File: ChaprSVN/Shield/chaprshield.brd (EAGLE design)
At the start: 72.7 x 47 mm, 16 parts, among them M2 RN42 Module

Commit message: First version of the ChapR board v0.2.  These files were sent to Sunstone.
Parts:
- removed U$1: VDIP2, ChapR-Custom:VDIP2
- removed U$3: PROMINI, ChapR-Custom:PROMINI
- added ARD: PROMINI, ChapR-Custom:PROMINI
- added JP1: (no value), pinhead:1X02
- added PB1: PUSHBUTTON, ChapR-Custom:2-PIN-PUSHBUTTON
- added R10, R11: 10k, resistor:0207/10
- added VDIP: VDIP2, ChapR-Custom:VDIP2
- moved R9 36.9 mm to (54.6, 36.8)
- moved LED2 31.2 mm to (69.8, 6.35)
- moved R3 26.4 mm to (54.6, 33.0), turned to 0 degrees
- moved LED1 22.9 mm to (69.8, 12.7)
- moved R8 19.1 mm to (44.5, 20.3)
- moved U$2 14.9 mm to (69.8, 36.8)
- moved R7 11.5 mm to (57.1, 20.3)
- moved M2 5.08 mm to (47.0, 10.2)
- moved R2 2.84 mm to (40.6, 30.5)
- moved R1 2.54 mm to (40.6, 35.6)
- moved R5 1.80 mm to (7.62, 16.5)
- moved R4 1.80 mm to (10.2, 14.0)
- moved R6 1.80 mm to (12.7, 11.4)
- moved - 1.53 mm to (64.6, 43.8)
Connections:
- new net N$22: JP1.1, M2.22, R11.2
- new net N$24: ARD.A0, PB1.P$2, R10.2
- net +9V: now also ARD.RAWV; no longer U$3.RAWV
- net 3.3V: now also JP1.2, VDIP.32, VDIP.38, VDIP.39; no longer U$1.32, U$1.38, U$1.39
- net GND: now also ARD.GND, ARD.GND2, R10.1, R11.1, VDIP.12, VDIP.13, VDIP.15, VDIP.26; no longer M2.25, M2.27, U$1.12, U$1.13, U$1.15, U$1.26, U$3.GND, U$3.GND2
- net LED1(BD5): now also VDIP.4; no longer U$1.4
- net LED2(BD6): now also VDIP.5; no longer U$1.5
- net N$1: now also ARD.VCC, PB1.P$1, VDIP.2, VDIP.3, VDIP.9; no longer U$1.2, U$1.3, U$1.9, U$3.VCC
- net N$10: now also ARD.D9, VDIP.18; no longer U$1.18, U$3.D9
- net N$11: now also ARD.D8, VDIP.17; no longer U$1.17, U$3.D8
- net N$12: now also ARD.D7, VDIP.16; no longer U$1.16, U$3.D7
- net N$13: now also ARD.D6, VDIP.14; no longer U$1.14, U$3.D6
- net N$14: now also ARD.D4; no longer U$3.D4
- net N$15: now also ARD.D3; no longer U$3.D3
- net N$18: now also ARD.A2; no longer U$3.A2
- net N$2: now also ARD.D10, VDIP.30; no longer U$1.30, U$3.D10
- net N$20: now also ARD.A1; no longer U$3.A1
- net N$21: now also ARD.A3; no longer U$3.A3
- net N$3: now also ARD.D13; no longer U$3.D13
- net N$4: now also ARD.D12; no longer U$3.D12
- net N$5: now also ARD.D11; no longer U$3.D11
- net N$8: now also ARD.D5; no longer U$3.D5
- net NC(1): now also VDIP.1; no longer U$1.1
- net NC(2): now also VDIP.40; no longer U$1.40
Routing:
- net N$24: track 0.00 -> 97.4 mm, vias 0 -> 2
- net 3.3V: track 51.4 -> 115.2 mm, vias 1 -> 2
- net N$1: track 42.4 -> 102.4 mm, vias 0 -> 2
- net N$22: track 0.00 -> 55.9 mm
- net N$21: track 9.87 -> 62.1 mm, vias 0 -> 2
- net N$9: track 43.8 -> 83.3 mm, vias 0 -> 4
- net N$2: track 57.9 -> 82.5 mm
- net N$19: track 38.0 -> 14.4 mm
- net N$20: track 57.3 -> 33.8 mm
- net GND: track 150.3 -> 171.8 mm
- net N$16: track 37.1 -> 20.6 mm
- net N$15: track 48.8 -> 39.0 mm, vias 0 -> 1
- net N$5: track 72.3 -> 63.2 mm, vias 0 -> 1
- net +9V: track 68.8 -> 60.6 mm, vias 0 -> 3
- net N$11: track 53.7 -> 60.6 mm
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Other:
- board size 72.7 x 47 mm -> 76 x 47 mm
- board text added: "ChapR v0.2"

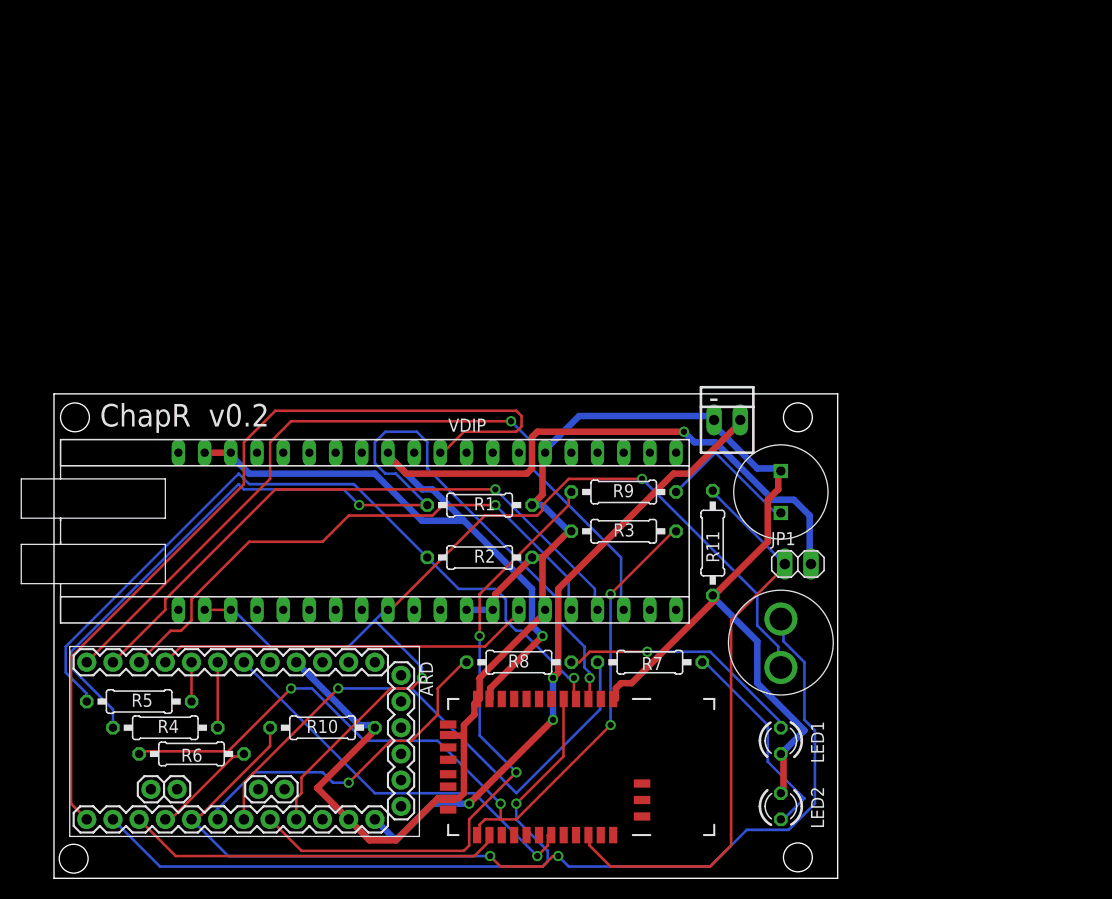
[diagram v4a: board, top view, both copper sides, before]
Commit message: 
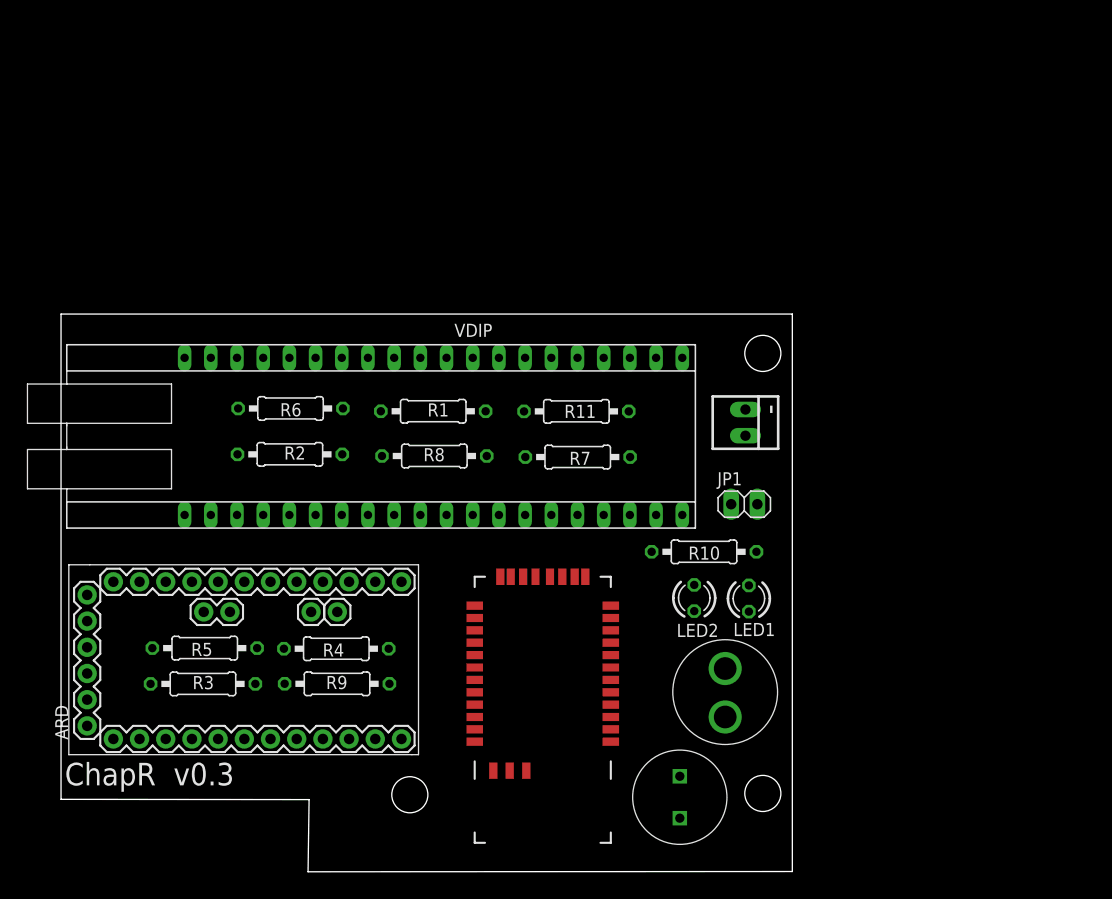
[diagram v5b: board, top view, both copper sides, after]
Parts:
- R1, R2, R3: value 20k -> 19.1k
- moved R3 43.4 mm to (13.8, 18.2)
- moved R10 40.7 mm to (62.4, 31.0), turned to 0 degrees
- moved R6 34.8 mm to (22.3, 44.9)
- moved R9 33.4 mm to (26.8, 18.2)
- moved U$2 31.2 mm to (60.0, 7.23)
- moved LED2 21.9 mm to (61.5, 26.6)
- moved R8 21.6 mm to (36.2, 40.3)
- moved R7 21.1 mm to (50.1, 40.2)
- moved R2 20.9 mm to (22.2, 40.5)
- moved R11 18.4 mm to (50.0, 44.6), turned to 180 degrees
- moved R4 18.3 mm to (26.7, 21.6), turned to 180 degrees
- moved LED1 14.1 mm to (66.8, 26.5), turned to 90 degrees
- moved ARD 10.3 mm to (17.8, 21.8), turned to 90 degrees
- moved R1 10.2 mm to (36.1, 44.7)
- moved VDIP 9.22 mm to (36.2, 42.2)
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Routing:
- net GND: track 171.8 -> 0.00 mm
- net 3.3V: track 115.2 -> 0.00 mm, vias 2 -> 0
- net N$1: track 102.4 -> 0.00 mm, vias 2 -> 0
- net N$6: track 97.4 -> 0.00 mm, vias 2 -> 0
- net N$24: track 97.4 -> 0.00 mm, vias 2 -> 0
- net N$9: track 83.3 -> 0.00 mm, vias 4 -> 0
- net N$2: track 82.5 -> 0.00 mm
- net N$10: track 75.9 -> 0.00 mm, vias 1 -> 0
- net N$7: track 74.0 -> 0.00 mm, vias 1 -> 0
- net N$5: track 63.2 -> 0.00 mm, vias 1 -> 0
- net N$21: track 62.1 -> 0.00 mm, vias 2 -> 0
- net +9V: track 60.6 -> 0.00 mm, vias 3 -> 0
- net N$11: track 60.6 -> 0.00 mm, vias 1 -> 0
- net N$22: track 55.9 -> 0.00 mm
- net N$12: track 55.4 -> 0.00 mm, vias 1 -> 0
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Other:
- board size 76 x 47 mm -> 70.9 x 54.1 mm
- board text added: "ChapR v0.3"
- board text removed: "ChapR v0.2"

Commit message: 
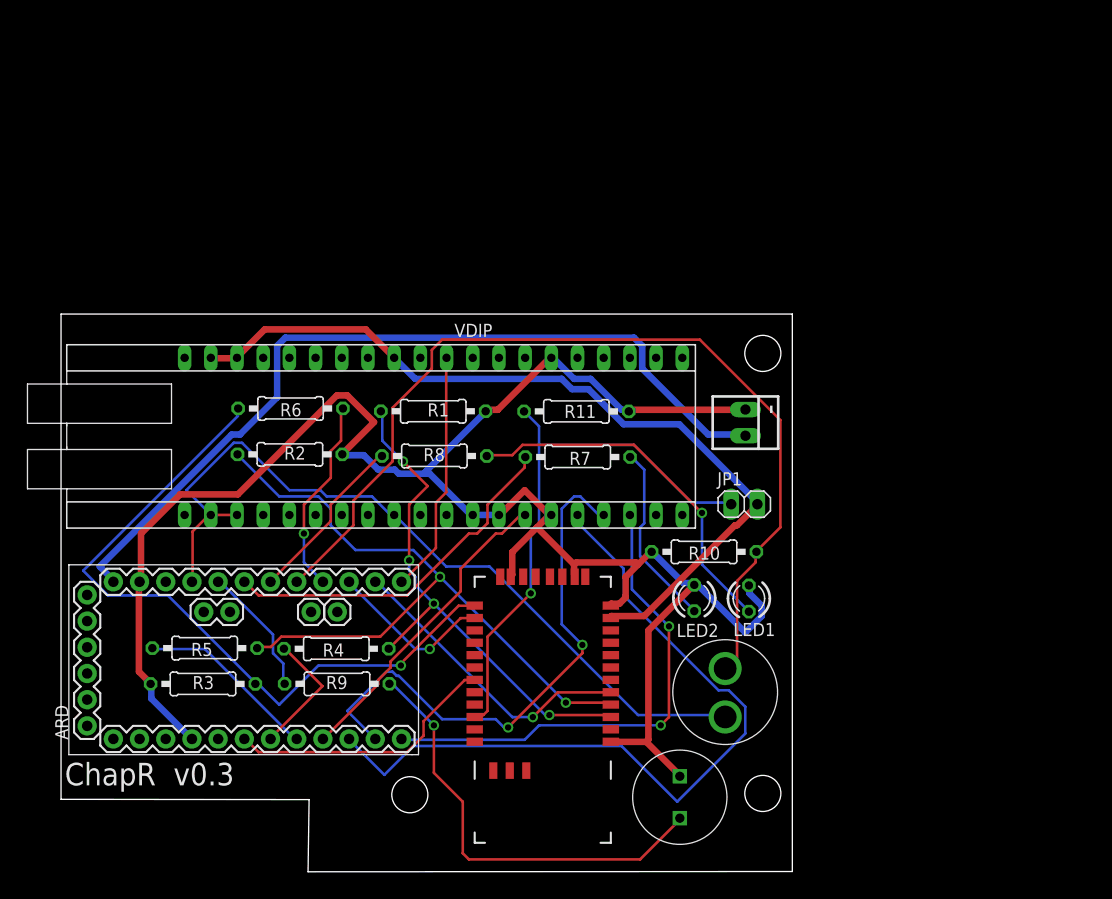
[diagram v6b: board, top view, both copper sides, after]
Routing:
- net GND: track 0.00 -> 189.9 mm
- net N$24: track 0.00 -> 91.7 mm
- net +9V: track 0.00 -> 82.1 mm
- net 3.3V: track 0.00 -> 80.3 mm
- net N$1: track 0.00 -> 78.5 mm
- net N$12: track 0.00 -> 74.6 mm
- net N$9: track 0.00 -> 69.6 mm, vias 0 -> 1
- net N$7: track 0.00 -> 67.8 mm, vias 0 -> 2
- net N$22: track 0.00 -> 54.4 mm, vias 0 -> 1
- net N$11: track 0.00 -> 53.6 mm, vias 0 -> 2
- net N$6: track 0.00 -> 50.2 mm, vias 0 -> 4
- net N$10: track 0.00 -> 48.2 mm, vias 0 -> 2
- net N$19: track 0.00 -> 42.6 mm, vias 0 -> 1
- net N$17: track 0.00 -> 35.5 mm, vias 0 -> 1
- net N$18: track 0.00 -> 35.0 mm
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
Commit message: Changes to keep vias away from bottom of BT module.
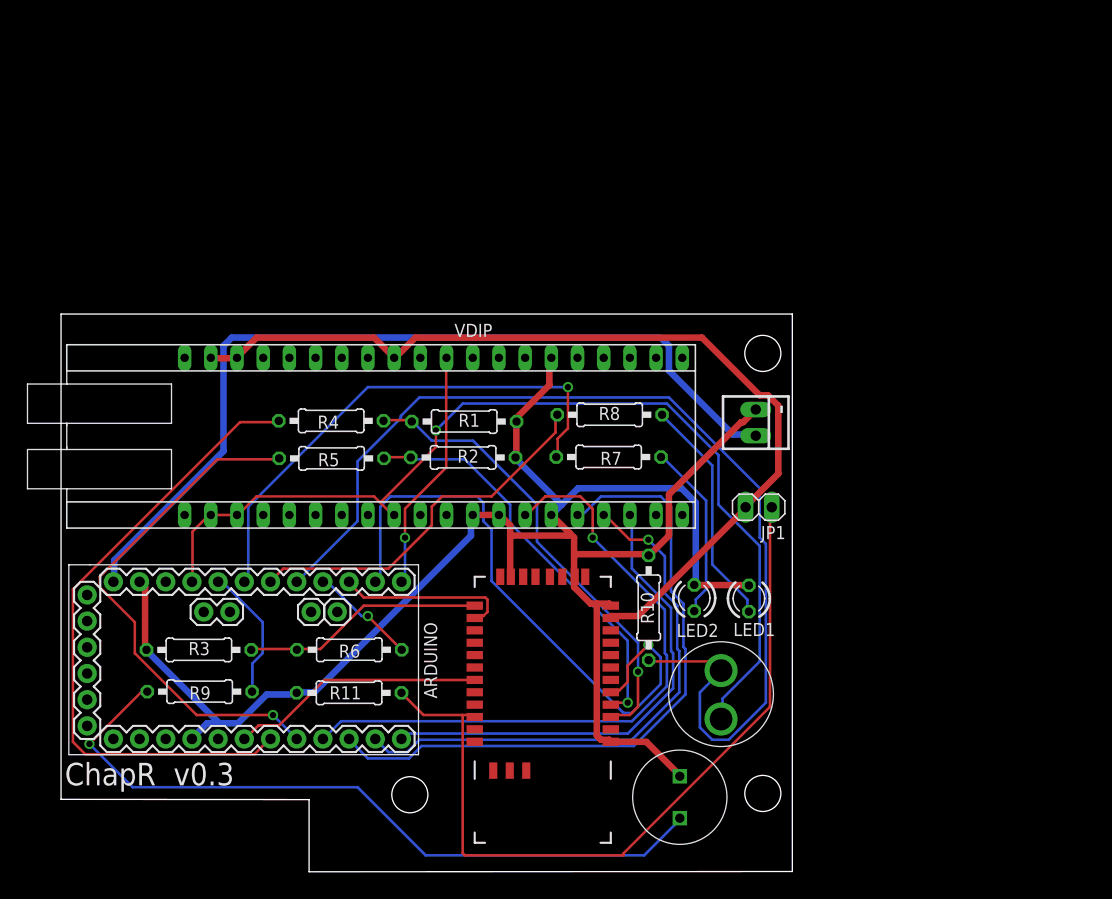
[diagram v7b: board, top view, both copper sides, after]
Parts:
- moved R11 35.1 mm to (28.0, 17.4), turned to 0 degrees
- moved R6 24.1 mm to (28.0, 21.5)
- moved R5 22.1 mm to (26.3, 40.1)
- moved R4 22.1 mm to (26.2, 43.7)
- moved R8 17.5 mm to (53.2, 44.3)
- moved R2 16.8 mm to (39.0, 40.2)
- moved R9 13.3 mm to (13.5, 17.5), turned to 0 degrees
- moved R10 7.64 mm to (57.0, 25.6), turned to 270 degrees
- moved R3 3.32 mm to (13.4, 21.5)
- moved R1 3.16 mm to (39.1, 43.7)
- moved R7 3.00 mm to (53.1, 40.2)
- moved JP1 1.43 mm to (67.7, 35.4), turned to 180 degrees
- moved - 1.00 mm to (67.4, 43.6)
- moved PB1 0.45 mm to (64.0, 16.6)
- renumbered ARD to ARDUINO
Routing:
- net N$14: track 12.4 -> 61.8 mm
- net N$9: track 69.6 -> 23.5 mm, vias 1 -> 0
- net N$13: track 30.5 -> 63.4 mm, vias 0 -> 1
- net N$8: track 17.7 -> 50.2 mm, vias 0 -> 1
- net N$5: track 29.3 -> 59.8 mm
- net N$19: track 42.6 -> 71.0 mm
- net N$7: track 67.8 -> 40.0 mm, vias 2 -> 1
- net N$22: track 54.4 -> 76.9 mm, vias 1 -> 0
- net N$20: track 16.8 -> 36.5 mm
- net N$1: track 78.5 -> 95.2 mm, vias 0 -> 1
- net N$18: track 35.0 -> 50.5 mm, vias 0 -> 1
- net GND: track 189.9 -> 176.5 mm
- net N$17: track 35.5 -> 22.6 mm, vias 1 -> 0
- net N$24: track 91.7 -> 102.7 mm
- net N$12: track 74.6 -> 65.0 mm
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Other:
- outline, holes or cut-outs redrawn
